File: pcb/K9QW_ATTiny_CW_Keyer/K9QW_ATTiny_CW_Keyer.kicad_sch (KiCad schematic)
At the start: 37 parts, among them J1 Power Input, J2 AudioJack4, J3 AudioJack4, J4 Sidetone, J5 Mounting Hole, Q1 AO3401A, Q2 MMBT2222A, Q3 MMBT3904, Q4 MMBT3904, SW1 Power Switch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

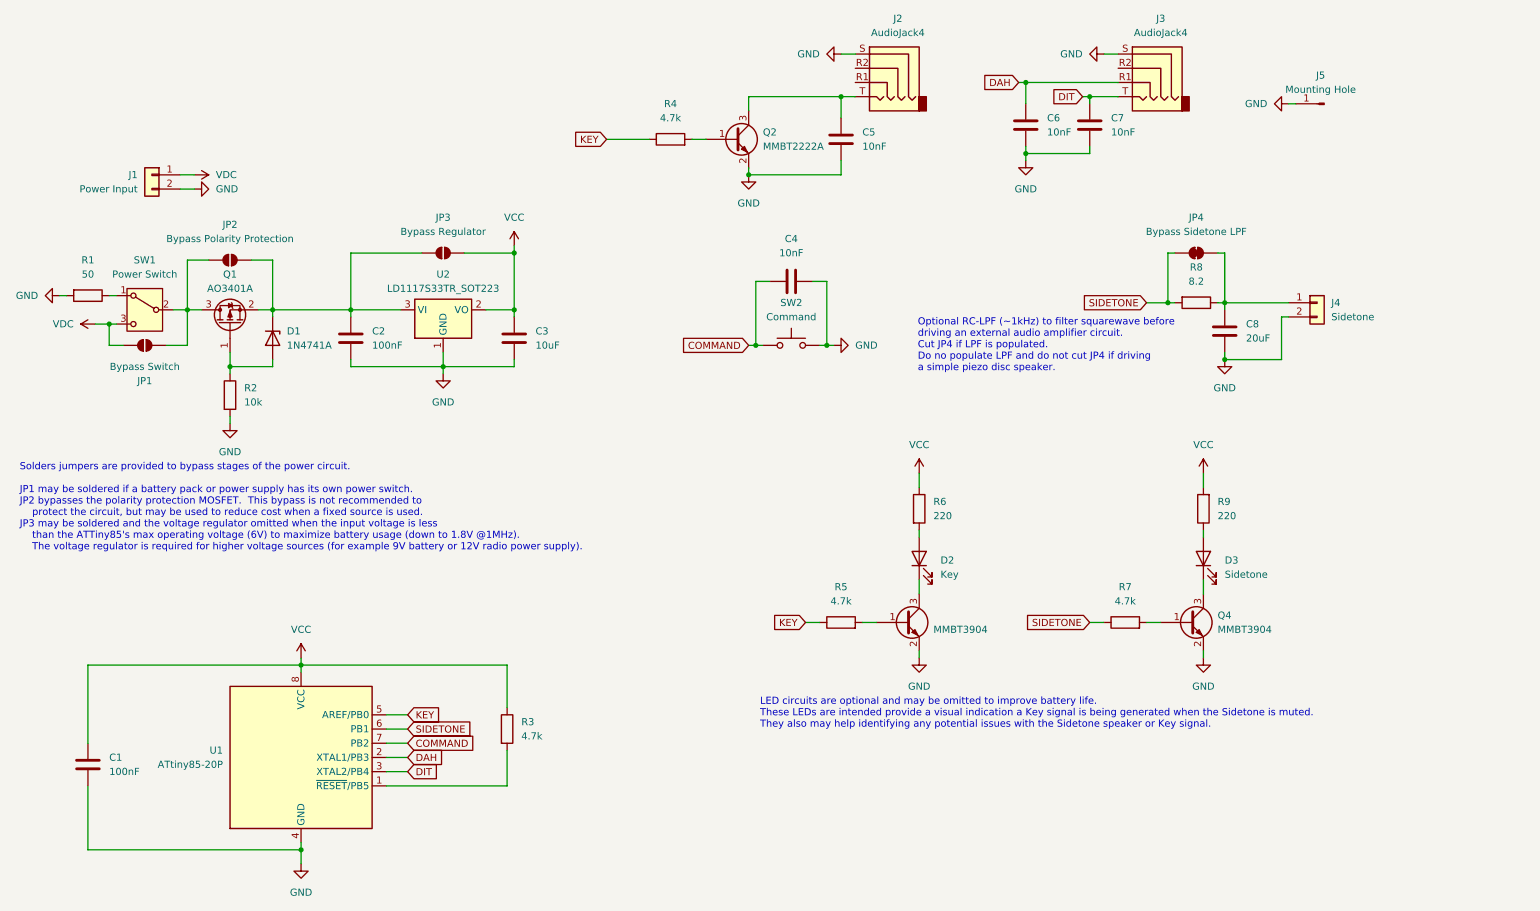
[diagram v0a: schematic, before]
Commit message: Adding power supply filter cap and preparing buzzer
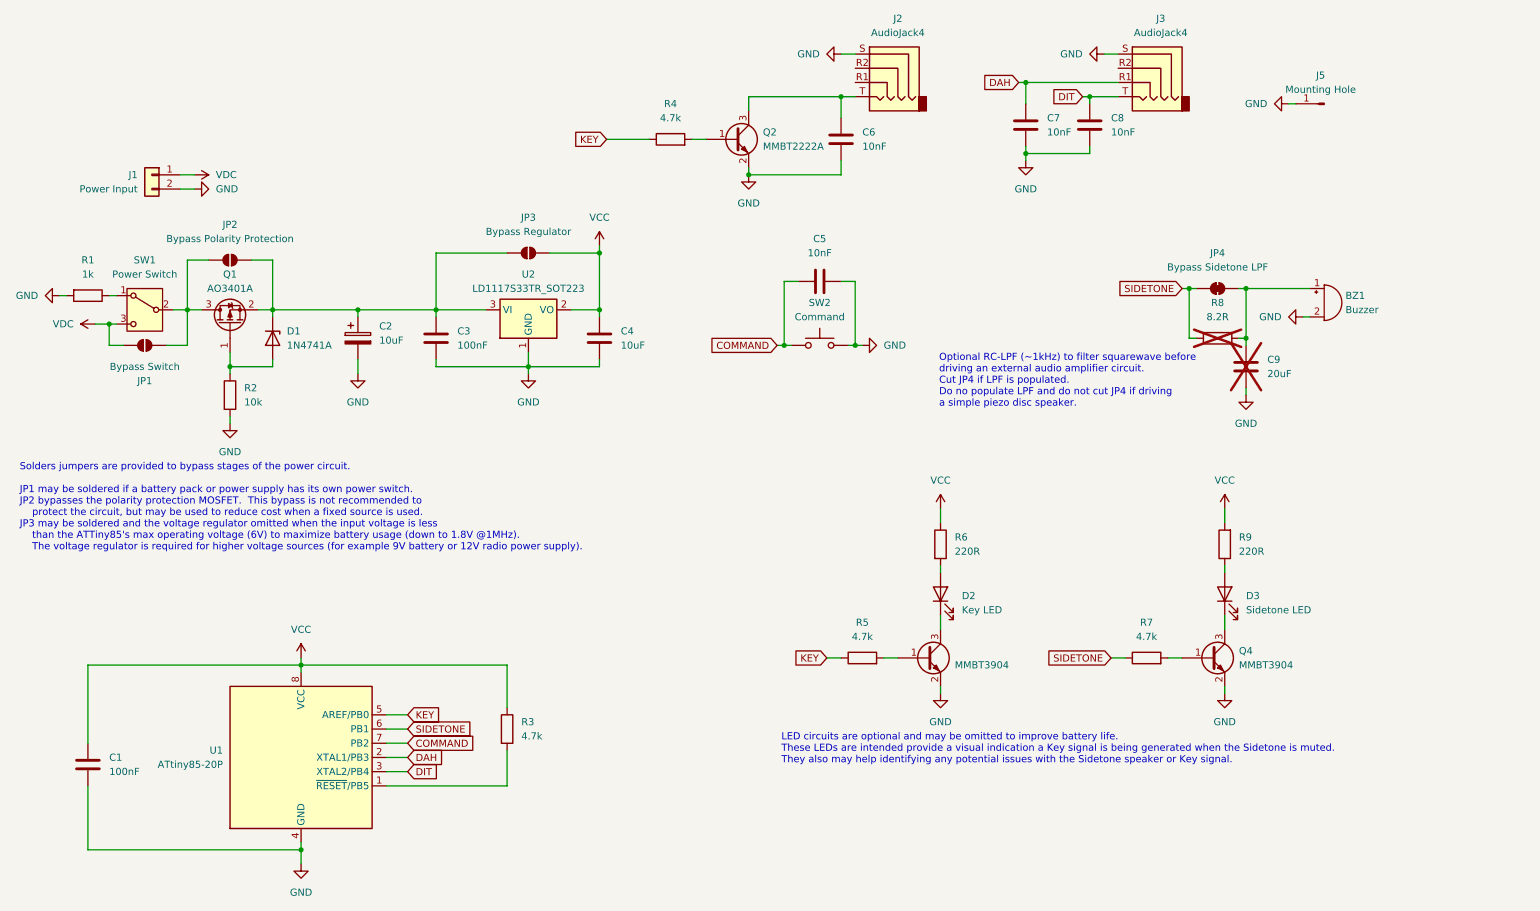
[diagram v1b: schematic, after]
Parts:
- removed J4: Sidetone, Connector_JST:JST_XH_B2B-XH-A_1x02_P2.50mm_Vertical, symbol Connector_Generic:Conn_01x02
- added BZ1: Buzzer, Buzzer_Beeper:Buzzer_TDK_PS1240P02BT_D12.2mm_H6.5mm, symbol Device:Buzzer
- added C2: 10uF, Capacitor_THT:CP_Radial_D5.0mm_P2.00mm, symbol Device:C_Polarized
- C9: renamed from C8; now not fitted
- D1: footprint Diode_THT:D_DO-41_SOD81_P10.16mm_Horizontal -> Diode_THT:D_DO-41_SOD81_P3.81mm_Vertical_KathodeUp
- D2: value Key -> Key LED
- D3: value Sidetone -> Sidetone LED
- R1: value 50 -> 1k
- R6, R9: value 220 -> 220R
- R8: value 8.2 -> 8.2R; now not fitted
- renumbered C2 to C3, C3 to C4, C4 to C5, C5 to C6, C6 to C7, C7 to C8
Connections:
- net GND: now also BZ1.2 (-), C2.2
- net at C3.1, D1.1 (K), JP2.2 (B)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: now also C2.1
- net at C9.1, JP4.2 (B), R8.1: now also BZ1.1 (+)
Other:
- moved on the sheet: C3, C4, C5, D2, D3, JP3, JP4, Q4, R5, R6, R7, R9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

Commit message: Refining routing
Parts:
- renumbered J5 to J4
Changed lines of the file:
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@@
 		)
 	)
-	(text "Solders jumpers are provided to bypass stages of the power circuit.\n\nJP1 may be soldered if a battery pack or power supply has its own power switch.\nJP2 bypasses the polarity protection MOSFET.  This bypass is not recommended to \n	protect the circuit, but may be used to reduce cost when a fixed source is used.\nJP3 may be soldered and the voltage regulator omitted when the input voltage is less \n	than the ATTiny85's max operating voltage (6V) to maximize battery usage (down to 1.8V @1MHz).\n	The voltage regulator is required for higher voltage sources (for example 9V battery or 12V radio power supply)."
+	(text "Solders jumpers are provided to bypass stages of the power circuit.\n\nJP1 may be soldered if a battery pack or power supply has its own power switch.\nJP2 bypasses the polarity protection MOSFET.  This bypass is not recommended to \n	protect the circuit, but may be used to reduce cost when a fixed source is used.\nJP3 may be soldered and the voltage regulator omitted when the input voltage is less \n	than the ATTiny85's max operating voltage (6V) to maximize battery usage (down to 1.8V @1MHz, LEDs may not light).\n	The voltage regulator is required for higher voltage sources (for example 9V battery or 12V radio power supply)."
 		(exclude_from_sim no)
 		(at 29.718 112.776 0)
@@
 		(dnp no)
 		(fields_autoplaced yes)
-		(property "Reference" "J5"
+		(property "Reference" "J4"
 			(at 262.255 35.56 0)
 			(effects
@@
 			(project ""
 				(path "/aef77cdf-c6ea-4cd5-9717-5394839cbff2"
-					(reference "J5")
+					(reference "J4")
 					(unit 1)
 				)
@@
 		(dnp no)
 		(fields_autoplaced yes)
-		(property "Reference" "#PWR013"
+		(property "Reference" "#PWR012"
 			(at 170.18 31.75 0)
 			(effects
@@
 			(project ""
 				(path "/aef77cdf-c6ea-4cd5-9717-5394839cbff2"
-					(reference "#PWR013")
+					(reference "#PWR012")
 					(unit 1)
 				)
@@
 		(dnp no)
 		(fields_autoplaced yes)
-		(property "Reference" "#PWR012"
+		(property "Reference" "#PWR013"
 			(at 186.69 83.82 0)
 			(effects
@@
 			(project "K9QW_ATTiny_CW_Keyer"
 				(path "/aef77cdf-c6ea-4cd5-9717-5394839cbff2"
-					(reference "#PWR012")
+					(reference "#PWR013")
 					(unit 1)
 				)

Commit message: Buffer for LPF
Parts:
- added U3: LM321, Package_TO_SOT_SMD:SOT-23-5, symbol Amplifier_Operational:LM321
- renumbered C9 to C7, C7 to C8, C8 to C9, R8 to R7, R7 to R8
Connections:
- net GND: now also U3.2 (V-)
- net VCC: now also U3.5 (V+)
- net at C7.1, R7.1: now also U3.1 (+); no longer BZ1.1 (+), JP4.2 (B)
- new net: BZ1.1 (+), JP4.2 (B), U3.3 (-), U3.4
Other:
- note added: "Optional RC-LPF (~1kHz) to filter squarewave before driving an external audio circuit. Cut JP4 if LPF is populated. Do no populate LPF and do not cut JP4 if driving a simple piezo disc speaker."
- note removed: "Optional RC-LPF (~1kHz) to filter squarewave before driving an external audio amplifier circuit. Cut JP4 if LPF is populated. Do no populate LPF and do not cut JP4 if driving a simple piezo disc speaker."
- moved on the sheet: BZ1, C5, C7, JP4, R7, SW2

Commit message: Adding resistor for 'charging and discharging to a piezoelectric element' as per buzzer datasheet.
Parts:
- added R10: 1k, Resistor_SMD:R_0603_1608Metric_Pad0.98x0.95mm_HandSolder, symbol Device:R
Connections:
- net GND: now also R10.2
- net at BZ1.1 (+), JP4.2 (B), U3.3 (-)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: now also R10.1
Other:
- moved on the sheet: BZ1
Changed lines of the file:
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@@
 	)
 	(junction
+		(at 245.11 66.04)
+		(diameter 0)
+		(color 0 0 0 0)
+	)
+	(junction
 		(at 176.53 39.37)
 		(diameter 0)
@@
 	)
 	(junction
-		(at 59.69 77.47)
+		(at 254 66.04)
 		(diameter 0)
 		(color 0 0 0 0)
 	)
 	(junction
-		(at 195.58 66.04)
+		(at 59.69 77.47)
 		(diameter 0)
 		(color 0 0 0 0)
 	)
 	(junction
-		(at 209.55 49.53)
+		(at 195.58 66.04)
 		(diameter 0)
 		(color 0 0 0 0)
 	)
 	(junction
-		(at 245.11 66.04)
+		(at 209.55 49.53)
 		(diameter 0)
 		(color 0 0 0 0)
@@
 	(wire
 		(pts
+			(xy 254 66.04) (xy 254 67.31)
+		)
+		(stroke
+			(width 0)
+			(type default)
+		)
+	)
+	(wire
+		(pts
 			(xy 71.12 68.58) (xy 74.93 68.58)
 		)
@@
 	(wire
 		(pts
-			(xy 245.11 66.04) (xy 256.54 66.04)
+			(xy 104.14 86.36) (xy 104.14 87.63)
 		)
 		(stroke
@@
 	(wire
 		(pts
-			(xy 104.14 86.36) (xy 104.14 87.63)
+			(xy 163.83 77.47) (xy 163.83 88.9)
 		)
 		(stroke
@@
 	(wire
 		(pts
-			(xy 163.83 77.47) (xy 163.83 88.9)
+			(xy 254 74.93) (xy 254 76.2)
 		)
 		(stroke
@@
 	(wire
 		(pts
+			(xy 254 66.04) (xy 270.51 66.04)
+		)
+		(stroke
+			(width 0)
+			(type default)
+		)
+	)
+	(wire
+		(pts
 			(xy 175.26 88.9) (xy 176.53 88.9)
 		)
@@
 	(wire
 		(pts
+			(xy 245.11 66.04) (xy 254 66.04)
+		)
+		(stroke
+			(width 0)
+			(type default)
+		)
+	)
+	(wire
+		(pts
 			(xy 195.58 66.04) (xy 195.58 80.01)
 		)
@@
 	(wire
 		(pts
-			(xy 256.54 71.12) (xy 255.27 71.12)
+			(xy 270.51 71.12) (xy 269.24 71.12)
 		)
 		(stroke
@@
 	(symbol
 		(lib_id "power:GND")
-		(at 255.27 71.12 270)
+		(at 269.24 71.12 270)
 		(unit 1)
 		(exclude_from_sim no)
@@
 		(dnp no)
 		(fields_autoplaced yes)
-		(property "Reference" "#PWR023"
-			(at 248.92 71.12 0)
+		(property "Reference" "#PWR025"
+			(at 262.89 71.12 0)
 			(effects
 				(font
@@
 		)
 		(property "Value" "GND"
-			(at 251.46 71.1199 90)
+			(at 265.43 71.1199 90)
 			(effects
 				(font
@@
 		)
 		(property "Footprint" ""
-			(at 255.27 71.12 0)
+			(at 269.24 71.12 0)
 			(effects
 				(font
@@
 		)
 		(property "Datasheet" ""
-			(at 255.27 71.12 0)
+			(at 269.24 71.12 0)
 			(effects
 				(font
@@
 		)
 		(property "Description" "Power symbol creates a global label with name \"GND\" , ground"
-			(at 255.27 71.12 0)
+			(at 269.24 71.12 0)
 			(effects
 				(font
@@
 			(project "K9QW_ATTiny_CW_Keyer"
 				(path "/aef77cdf-c6ea-4cd5-9717-5394839cbff2"
-					(reference "#PWR023")
+					(reference "#PWR025")
 					(unit 1)
 				)
@@
 	(symbol
 		(lib_id "power:GND")
+		(at 254 76.2 0)
+		(unit 1)
+		(exclude_from_sim no)
+		(in_bom yes)
+		(on_board yes)
+		(dnp no)
+		(fields_autoplaced yes)
+		(property "Reference" "#PWR023"
+			(at 254 82.55 0)
+			(effects
+				(font
+					(size 1.27 1.27)
+				)
+				(hide yes)
+			)
+		)
+		(property "Value" "GND"
+			(at 254 81.28 0)
+			(effects
+				(font
+					(size 1.27 1.27)
+				)
+			)
+		)
+		(property "Footprint" ""
+			(at 254 76.2 0)
+			(effects
+				(font
+					(size 1.27 1.27)
+				)
+				(hide yes)
+			)
+		)
+		(property "Datasheet" ""
+			(at 254 76.2 0)
+			(effects
+				(font
+					(size 1.27 1.27)
+				)
+				(hide yes)
+			)
+		)
+		(property "Description" "Power symbol creates a global label with name \"GND\" , ground"
+			(at 254 76.2 0)
+			(effects
+				(font
+					(size 1.27 1.27)
+				)
+				(hide yes)
+			)
+		)
+		(pin "1"
+		)
+		(instances
+			(project "K9QW_ATTiny_CW_Keyer"
+				(path "/aef77cdf-c6ea-4cd5-9717-5394839cbff2"
+					(reference "#PWR023")
+					(unit 1)
+				)
+			)
+		)
+	)
+	(symbol
+		(lib_id "power:GND")
 		(at 160.02 53.34 0)
 		(unit 1)
@@
 	)
 	(symbol
+		(lib_id "Device:R")
+		(at 254 71.12 0)
+		(unit 1)
+		(exclude_from_sim no)
+		(in_bom yes)
+		(on_board yes)
+		(dnp no)
+		(fields_autoplaced yes)
+		(property "Reference" "R10"
+			(at 256.54 69.8499 0)
+			(effects
+				(font
+					(size 1.27 1.27)
+				)
+				(justify left)
+			)
+		)
+		(property "Value" "1k"
+			(at 256.54 72.3899 0)
+			(effects
+				(font
+					(size 1.27 1.27)
+				)
+				(justify left)
+			)
+		)
+		(property "Footprint" "Resistor_SMD:R_0603_1608Metric_Pad0.98x0.95mm_HandSolder"
+			(at 252.222 71.12 90)
+			(effects
+				(font
+					(size 1.27 1.27)
+				)
+				(hide yes)
+			)
+		)
+		(property "Datasheet" "~"
+			(at 254 71.12 0)
+			(effects
+				(font
+					(size 1.27 1.27)
+				)
+				(hide yes)
+			)
+		)
+		(property "Description" "Resistor"
+			(at 254 71.12 0)
+			(effects
+				(font
+					(size 1.27 1.27)
+				)
+				(hide yes)
+			)
+		)
+		(pin "1"
+		)
+		(pin "2"
+		)
+		(instances
+			(project "K9QW_ATTiny_CW_Keyer"
+				(path "/aef77cdf-c6ea-4cd5-9717-5394839cbff2"
+					(reference "R10")
+					(unit 1)
+				)
+			)
+		)
+	)
+	(symbol
 		(lib_id "power:GND")
 		(at 80.01 176.53 0)
@@
 	(symbol
 		(lib_id "Device:Buzzer")
-		(at 259.08 68.58 0)
+		(at 273.05 68.58 0)
 		(unit 1)
 		(exclude_from_sim no)
@@
 		(fields_autoplaced yes)
 		(property "Reference" "BZ1"
-			(at 262.89 67.3099 0)
+			(at 276.86 67.3099 0)
 			(effects
 				(font
@@
 		)
 		(property "Value" "Buzzer"
-			(at 262.89 69.8499 0)
+			(at 276.86 69.8499 0)
 			(effects
 				(font
@@
 		)
 		(property "Footprint" "Buzzer_Beeper:Buzzer_TDK_PS1240P02BT_D12.2mm_H6.5mm"
-			(at 258.445 66.04 90)
+			(at 272.415 66.04 90)
 			(effects
 				(font
@@
 		)
 		(property "Datasheet" "~"
-			(at 258.445 66.04 90)
+			(at 272.415 66.04 90)
 			(effects
 				(font
@@
 		)
 		(property "Description" "Buzzer, polarized"
-			(at 259.08 68.58 0)
+			(at 273.05 68.58 0)
 			(effects
 				(font
